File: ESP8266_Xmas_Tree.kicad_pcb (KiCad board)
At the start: 2 copper layers, 158.7 x 185.8 mm, 44 parts, among them U1 WeMos_D1_mini

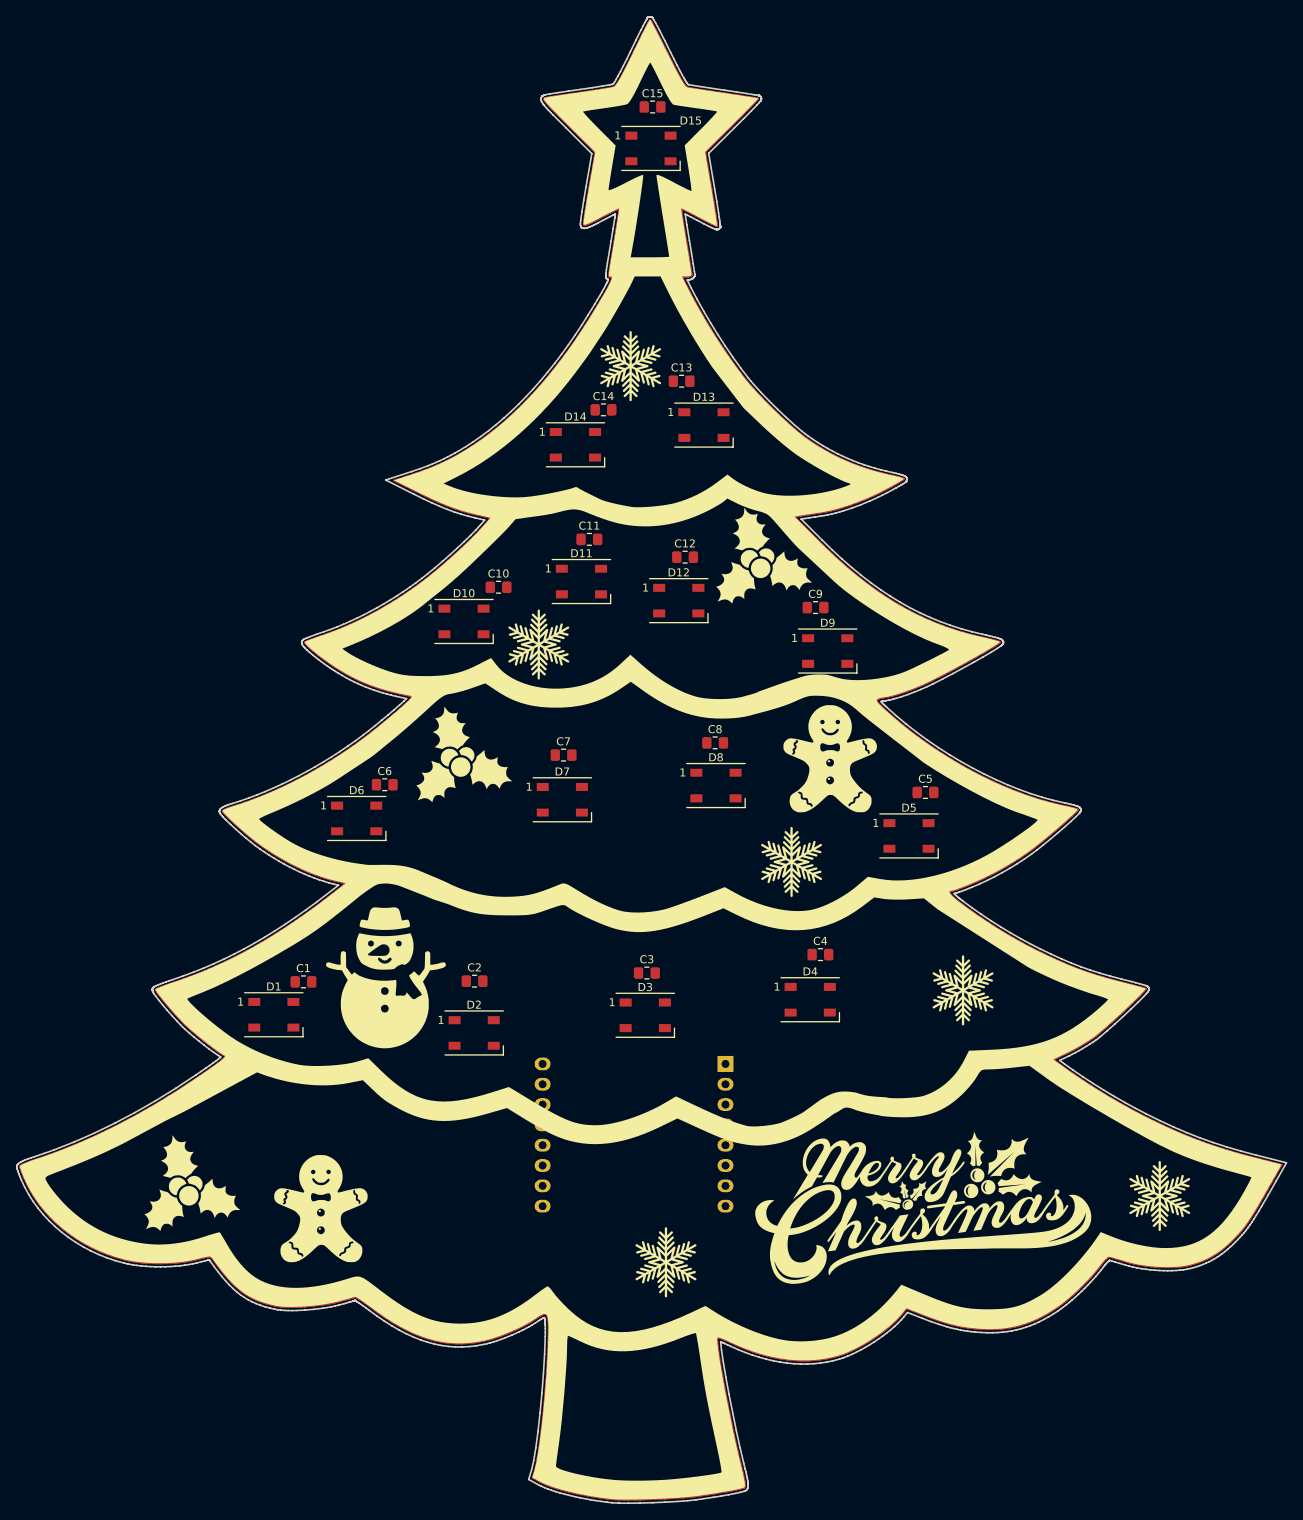
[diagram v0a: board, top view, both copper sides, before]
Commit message: adding Xmas balls, canes and santa claus to PCB in silkscreen
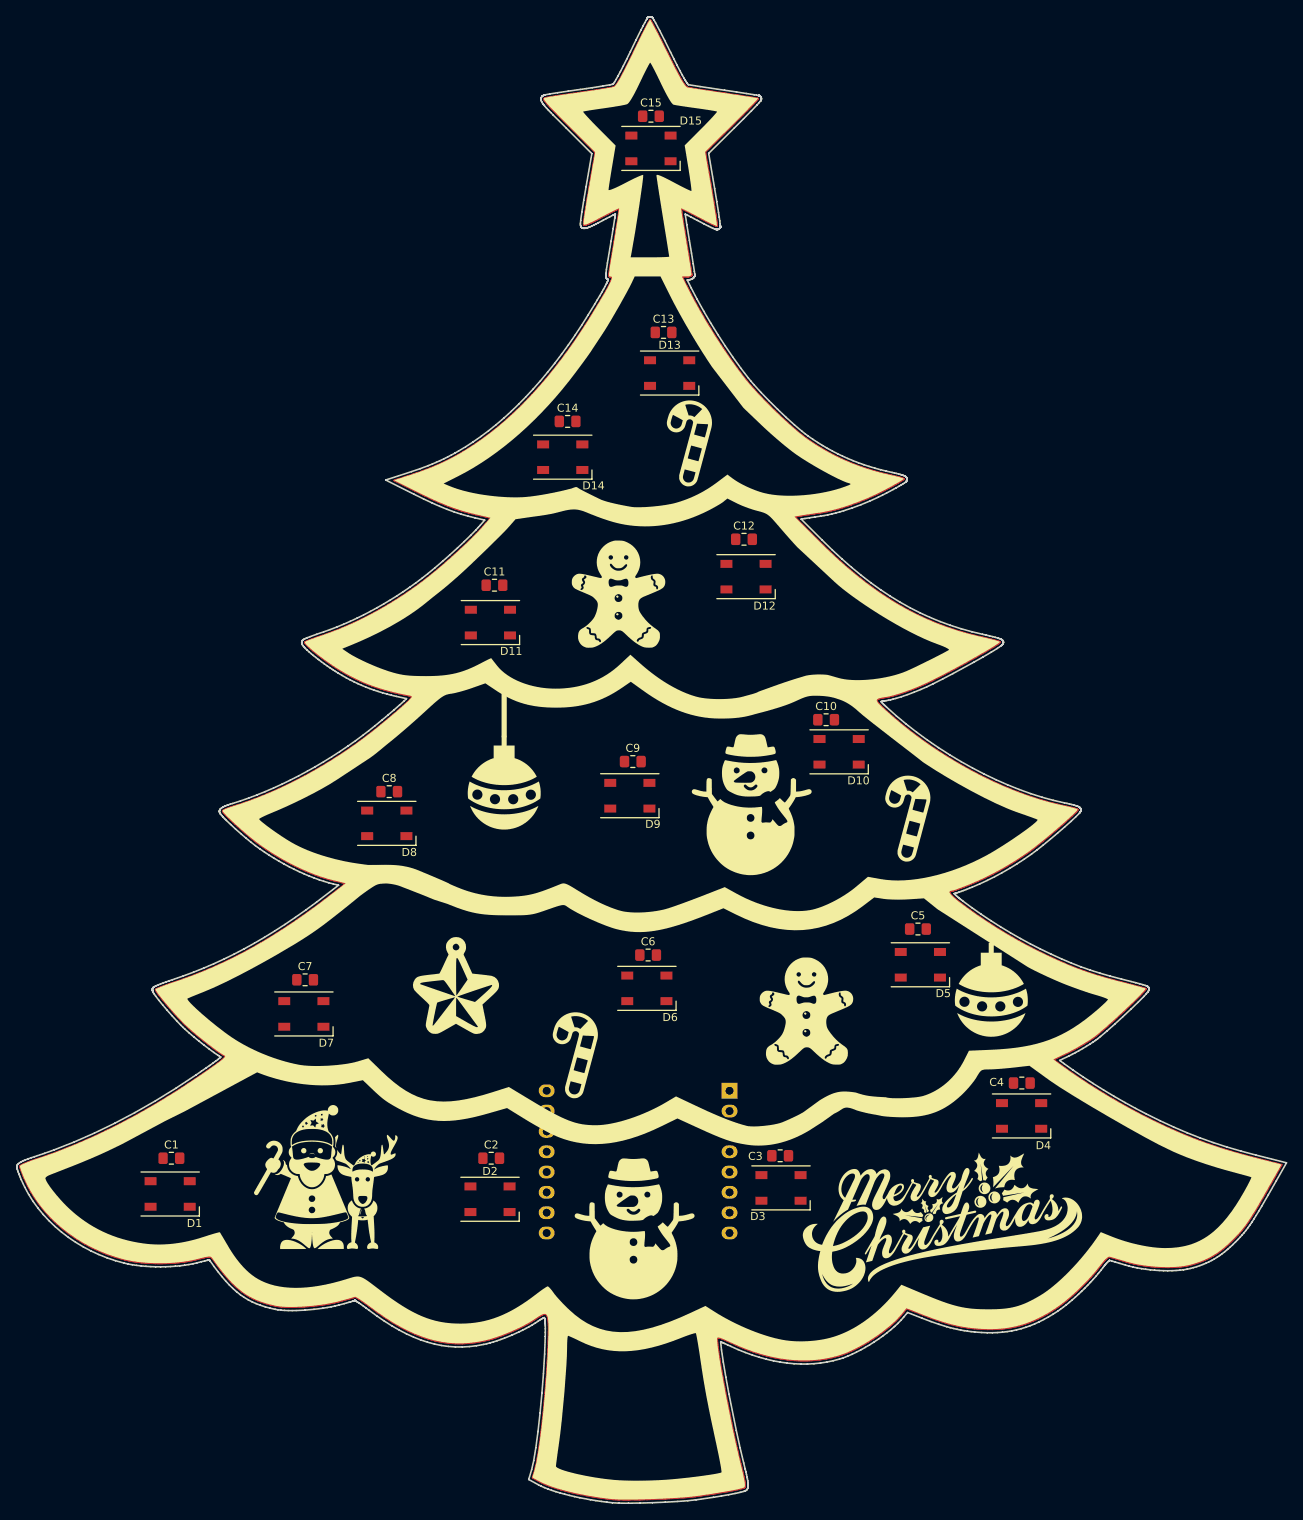
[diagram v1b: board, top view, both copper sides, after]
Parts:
- removed the G*** at (218.8, 157.3)
- removed the G*** at (264.9, 199.1)
- removed the G*** at (198.7, 95.4)
- removed the G*** at (240.3, 173.4)
- removed the G*** at (187.2, 130.1)
- removed the G*** at (235.3, 200.6)
- removed the G*** at (215.4, 119.0)
- removed the G*** at (203.1, 207.4)
- removed the G*** at (144.0, 197.5)
- removed the G*** at (178.0, 143.9)
- added G***: LOGO, LOGO, F.Cu at (206.1, 104.8)
- added G***: LOGO, LOGO, F.Cu at (191.8, 181.3)
- added G***: LOGO, LOGO, F.Cu at (213.9, 150.2)
- added G***: LOGO, LOGO, F.Cu at (160.6, 196.7)
- added G***: LOGO, LOGO, F.Cu at (176.9, 172.7)
- added G***: LOGO, LOGO, F.Cu at (233.4, 151.7)
- added G***: LOGO, LOGO, F.Cu at (237.6, 202.0)
- moved G*** 65.5 mm to (220.7, 175.8)
- moved D10 49.6 mm to (224.8, 143.6)
- moved G*** 44.2 mm to (199.2, 203.2)
- moved C10 44.2 mm to (223.2, 139.5)
- moved C7 42.8 mm to (158.0, 172.1)
- moved D6 42.0 mm to (200.8, 173.1)
- moved D7 42.0 mm to (157.9, 176.3)
- moved D8 41.4 mm to (168.2, 152.5)
- moved C8 41.2 mm to (168.6, 148.5)
- moved C6 39.2 mm to (200.9, 169.0)
- moved G*** 33.5 mm to (197.2, 123.7)
- moved D9 30.6 mm to (198.6, 149.0)
- moved D4 30.1 mm to (247.6, 189.1)
- moved C9 29.9 mm to (199.0, 144.8)
- moved C4 29.9 mm to (247.6, 185.0)
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
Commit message: Fix the naming error of the capacitors and change the supply voltage from 3V3 to 5V of the LEDs.
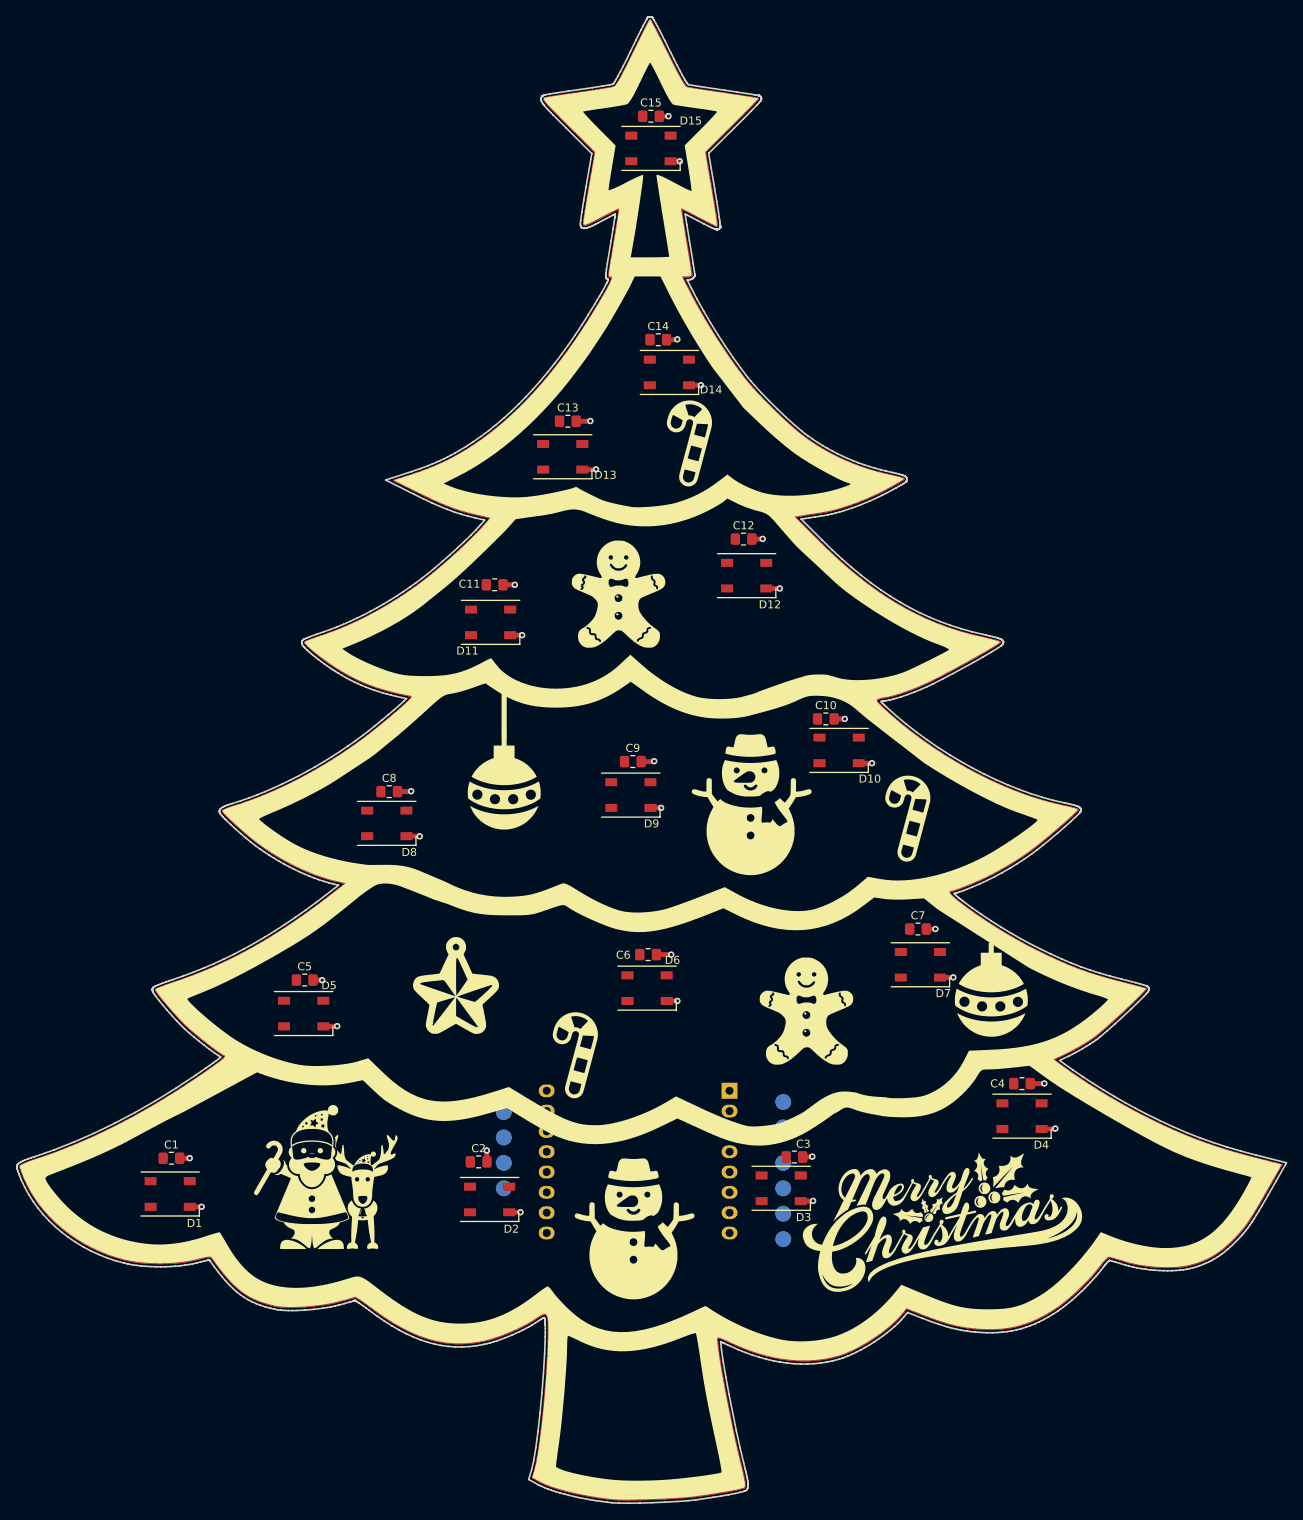
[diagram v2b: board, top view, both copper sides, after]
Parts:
- added TP1: TestPoint_Small, TestPoint:TestPoint_Pad_D2.0mm, B.Cu at (217.8, 187.3)
- added TP10: TestPoint_Small, TestPoint:TestPoint_Pad_D2.0mm, B.Cu at (217.8, 204.5)
- added TP2: TestPoint_Small, TestPoint:TestPoint_Pad_D2.0mm, B.Cu at (217.8, 190.5)
- added TP3: TestPoint_Small, TestPoint:TestPoint_Pad_D2.0mm, B.Cu at (182.9, 188.6)
- added TP4: TestPoint_Small, TestPoint:TestPoint_Pad_D2.0mm, B.Cu at (182.9, 191.8)
- added TP5: TestPoint_Small, TestPoint:TestPoint_Pad_D2.0mm, B.Cu at (182.9, 194.9)
- added TP6: TestPoint_Small, TestPoint:TestPoint_Pad_D2.0mm, B.Cu at (182.9, 198.1)
- added TP7: TestPoint_Small, TestPoint:TestPoint_Pad_D2.0mm, B.Cu at (217.8, 194.9)
- added TP8: TestPoint_Small, TestPoint:TestPoint_Pad_D2.0mm, B.Cu at (217.8, 198.1)
- added TP9: TestPoint_Small, TestPoint:TestPoint_Pad_D2.0mm, B.Cu at (217.8, 201.3)
- C1, C15, C2, C8: value C -> 100n
- C10: renamed from C14; value C -> 100n
- C11: renamed from C4; value C -> 100n
- C12: renamed from C6; value C -> 100n
- C13: renamed from C9; value C -> 100n
- C14: renamed from C12; value C -> 100n
- C3: renamed from C7; value C -> 100n
- C4: renamed from C10; value C -> 100n
- C5: renamed from C13; value C -> 100n
- C6: renamed from C3; value C -> 100n
- C7: renamed from C5; value C -> 100n
- C9: renamed from C11; value C -> 100n
- moved C5 92.5 mm to (158.0, 172.1)
- moved D5 92.2 mm to (157.9, 176.3)
- moved C11 90.7 mm to (181.7, 122.7)
- moved D11 79.5 mm to (181.2, 127.4)
- moved D2 67.3 mm to (181.1, 199.5)
- moved C3 65.1 mm to (219.2, 194.2)
- moved D3 63.5 mm to (217.6, 198.1)
- moved C12 53.3 mm to (212.9, 117.0)
- moved D12 53.1 mm to (213.2, 121.5)
- moved C4 51.7 mm to (247.7, 185.0)
- moved D4 51.0 mm to (247.7, 189.1)
- moved D10 50.4 mm to (224.8, 143.4)
- moved C10 49.2 mm to (223.1, 139.4)
- moved C13 43.3 mm to (190.9, 102.2)
- moved D13 43.2 mm to (190.2, 106.7)
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- renumbered D14 to D10, D3 to D11, D6 to D12, D9 to D13, D12 to D14, D4 to D2, D7 to D3, D10 to D4, D13 to D5, D2 to D6, D5 to D7, D11 to D9
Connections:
- C1 pad 1: +3.3V -> +5V
- C10 pad 1: +3.3V -> +5V
- C11 pad 1: +3.3V -> +5V
- C12 pad 1: +3.3V -> +5V
- C13 pad 1: +3.3V -> +5V
- C14 pad 1: +3.3V -> +5V
- C15 pad 1: +3.3V -> +5V
- C2 pad 1: +3.3V -> +5V
- C3 pad 1: +3.3V -> +5V
- C4 pad 1: +3.3V -> +5V
- C5 pad 1: +3.3V -> +5V
- C6 pad 1: +3.3V -> +5V
- C7 pad 1: +3.3V -> +5V
- C8 pad 1: +3.3V -> +5V
- C9 pad 1: +3.3V -> +5V
- D1 pad 1: +3.3V -> +5V
- D1 pad 4: unconnected-(D1-Pad4) -> /WS2812B_DIN
- D10 pad 1: +3.3V -> +5V
- D11 pad 1: +3.3V -> +5V
- D12 pad 1: +3.3V -> +5V
- D13 pad 1: +3.3V -> +5V
- D14 pad 1: +3.3V -> +5V
- D15 pad 1: +3.3V -> +5V
- D2 pad 1: +3.3V -> +5V
- D3 pad 1: +3.3V -> +5V
- D4 pad 1: +3.3V -> +5V
- D5 pad 1: +3.3V -> +5V
- D6 pad 1: +3.3V -> +5V
- D7 pad 1: +3.3V -> +5V
- D8 pad 1: +3.3V -> +5V
- D9 pad 1: +3.3V -> +5V
- U1 pad 11: unconnected-(U1-Pad11) -> /WS2812B_DIN
- U1 pad 12: unconnected-(U1-Pad12) -> Net-(U1-Pad12)
- U1 pad 13: unconnected-(U1-Pad13) -> Net-(U1-Pad13)
- U1 pad 14: unconnected-(U1-Pad14) -> Net-(U1-Pad14)
- U1 pad 2: unconnected-(U1-Pad2) -> Net-(U1-Pad2)
- U1 pad 3: unconnected-(U1-Pad3) -> Net-(U1-Pad3)
- U1 pad 4: unconnected-(U1-Pad4) -> /SCL
- U1 pad 5: unconnected-(U1-Pad5) -> /SDA
- U1 pad 6: unconnected-(U1-Pad6) -> Net-(U1-Pad6)
- U1 pad 7: unconnected-(U1-Pad7) -> Net-(U1-Pad7)
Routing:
- net GND: track 0.00 -> 44.8 mm, vias 1 -> 30
- added copper zone on F.Cu, net +5V
- removed copper zone on F.Cu, net GND

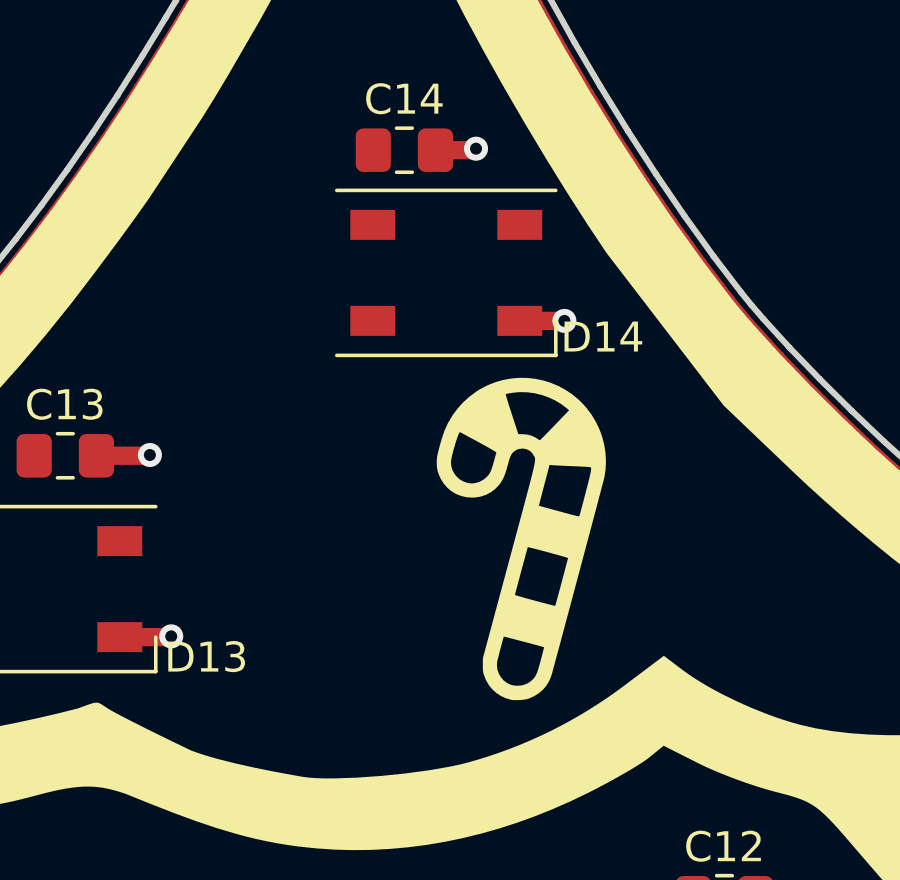
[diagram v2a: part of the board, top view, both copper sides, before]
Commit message: adding BMP280 Breakoutboard Lib and footprint to PCB
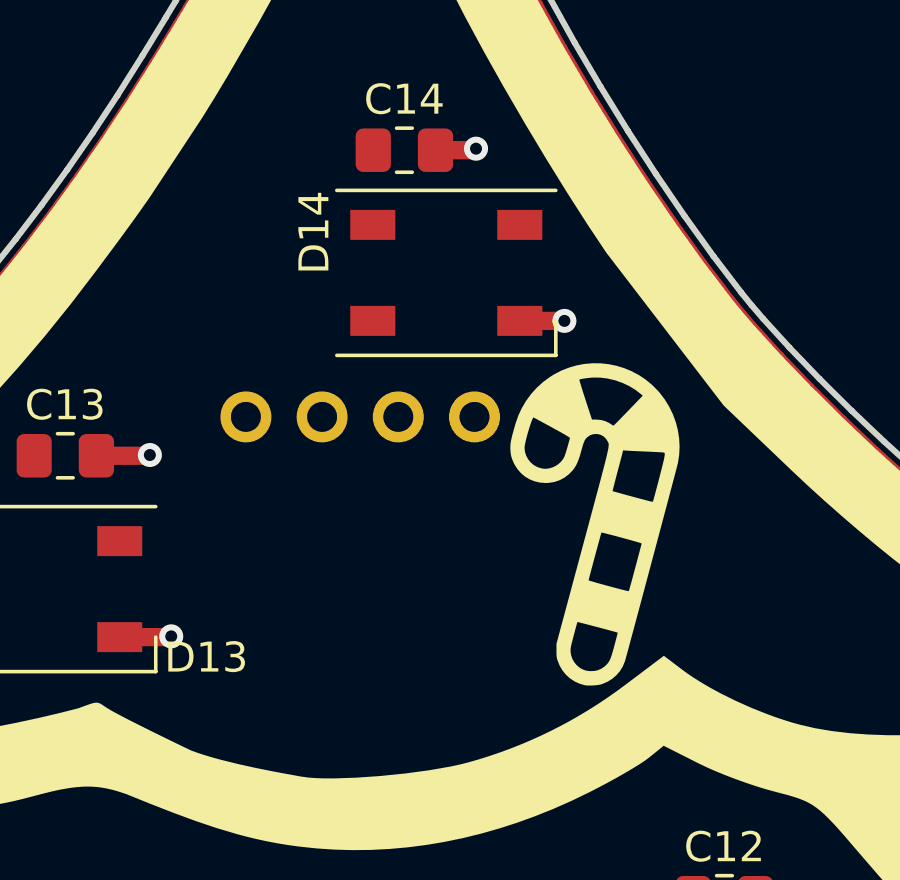
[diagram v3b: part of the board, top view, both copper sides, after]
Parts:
- added U2: BMP280_Breakoutboard, BMP280_Breakoutboard:BMP280_Breakoutboard, B.Cu at (204.5, 100.9)
- moved G*** 2.50 mm to (208.5, 104.3)

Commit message: first routing
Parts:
- added REF**: OSHW-Logo2_14.6x12mm_SilkScreen, Symbol:OSHW-Logo2_14.6x12mm_SilkScreen, B.Cu at (169.0, 189.6)
- added REF**: KiCad-Logo2_8mm_SilkScreen, Symbol:KiCad-Logo2_8mm_SilkScreen, B.Cu at (186.6, 128.5)
- moved C7 78.4 mm to (156.5, 172.3)
- moved D5 77.4 mm to (235.0, 169.9)
- moved D7 77.3 mm to (157.9, 176.3)
- moved C5 75.8 mm to (233.6, 165.9)
- moved D2 39.9 mm to (141.2, 198.7)
- moved C2 39.9 mm to (139.8, 194.8)
- moved D1 38.5 mm to (179.7, 199.6)
- moved C1 36.9 mm to (178.2, 195.3)
- moved C12 33.6 mm to (179.9, 123.3)
- moved D11 32.4 mm to (213.2, 121.6)
- moved D12 32.4 mm to (181.3, 127.4)
- moved C11 30.4 mm to (211.7, 117.7)
- moved U2 9.39 mm to (204.8, 110.3)
- moved C13 2.16 mm to (188.8, 102.7)
- moved C8 1.73 mm to (166.8, 148.4)
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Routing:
- net +3.3V: track 0.00 -> 104.7 mm, vias 0 -> 2
- net /SDA: track 0.00 -> 99.8 mm
- net /SCL: track 0.00 -> 95.8 mm
- net Net-(D2-Pad2): track 0.00 -> 86.4 mm
- net Net-(D3-Pad2): track 0.00 -> 44.6 mm
- net Net-(D7-Pad2): track 0.00 -> 39.4 mm
- net Net-(D8-Pad2): track 0.00 -> 39.2 mm
- net Net-(D10-Pad2): track 0.00 -> 38.8 mm
- net Net-(D6-Pad2): track 0.00 -> 38.0 mm
- net Net-(D10-Pad4): track 0.00 -> 37.3 mm
- net Net-(D14-Pad2): track 0.00 -> 36.7 mm
- net Net-(D1-Pad2): track 0.00 -> 35.3 mm
- net Net-(D12-Pad2): track 0.00 -> 35.1 mm
- net Net-(D4-Pad2): track 0.00 -> 31.4 mm
- net Net-(D5-Pad2): track 0.00 -> 29.3 mm
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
